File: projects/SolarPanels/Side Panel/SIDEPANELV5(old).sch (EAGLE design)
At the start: 31 parts

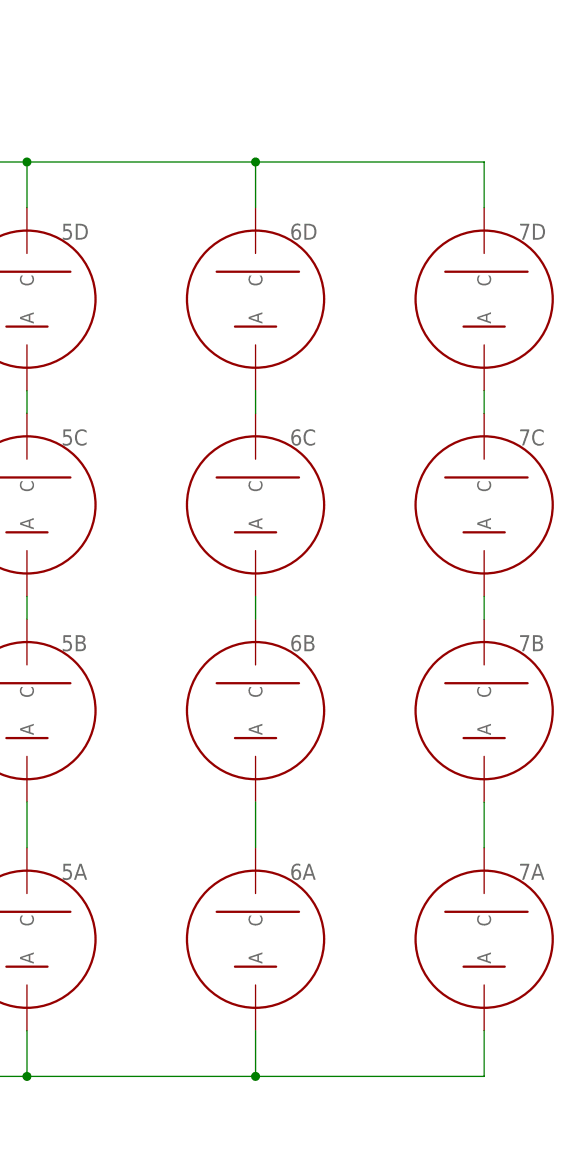
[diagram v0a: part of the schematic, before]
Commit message: side panel v5 WIP
updated cells
still figuring out cell layout
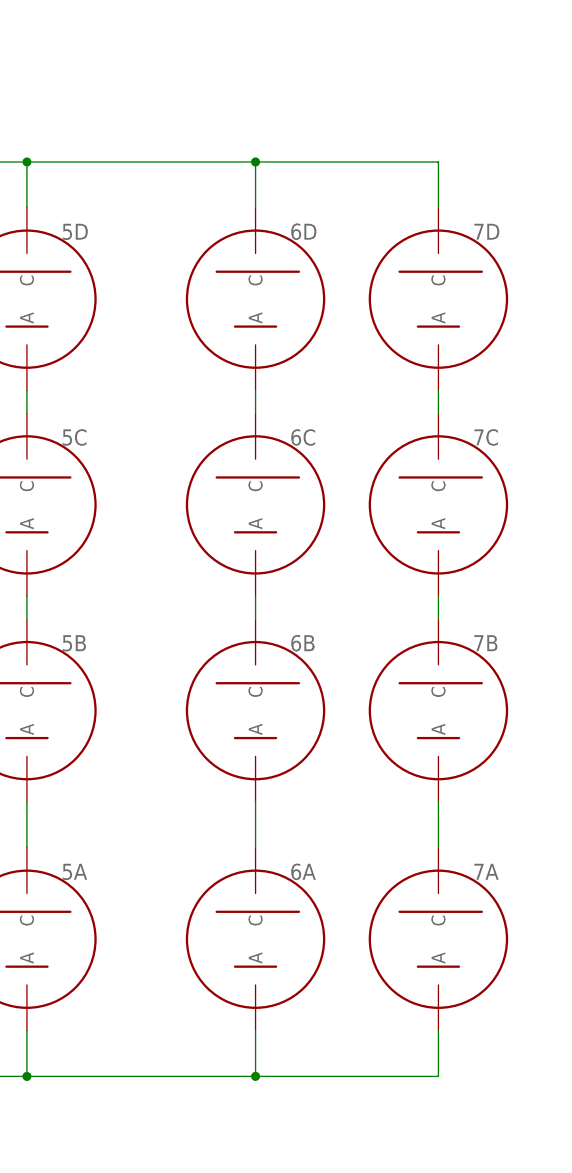
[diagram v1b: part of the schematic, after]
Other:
- moved on the sheet: 7A, 7B, 7C, 7D
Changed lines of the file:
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@@
 <?xml version="1.0" encoding="utf-8"?>
 <!DOCTYPE eagle SYSTEM "eagle.dtd">
-<eagle version="8.2.2">
+<eagle version="8.0.0">
 <drawing>
 <settings>
@@
 <instance part="6A" gate="G$1" x="17.78" y="-25.4"/>
 <instance part="PD" gate="G$1" x="-33.02" y="106.68"/>
-<instance part="7D" gate="G$1" x="43.18" y="45.72"/>
-<instance part="7C" gate="G$1" x="43.18" y="22.86"/>
-<instance part="7B" gate="G$1" x="43.18" y="0"/>
-<instance part="7A" gate="G$1" x="43.18" y="-25.4"/>
+<instance part="7D" gate="G$1" x="38.1" y="45.72"/>
+<instance part="7C" gate="G$1" x="38.1" y="22.86"/>
+<instance part="7B" gate="G$1" x="38.1" y="0"/>
+<instance part="7A" gate="G$1" x="38.1" y="-25.4"/>
 </instances>
 <busses>
@@
 <wire x1="-116.84" y1="-35.56" x2="-116.84" y2="-40.64" width="0.1524" layer="91"/>
 <pinref part="7A" gate="G$1" pin="A"/>
-<wire x1="17.78" y1="-40.64" x2="43.18" y2="-40.64" width="0.1524" layer="91"/>
-<wire x1="43.18" y1="-35.56" x2="43.18" y2="-40.64" width="0.1524" layer="91"/>
+<wire x1="38.1" y1="-35.56" x2="38.1" y2="-40.64" width="0.1524" layer="91"/>
+<wire x1="38.1" y1="-40.64" x2="17.78" y2="-40.64" width="0.1524" layer="91"/>
 <junction x="17.78" y="-40.64"/>
 </segment>
@@
 <wire x1="-60.96" y1="55.88" x2="-60.96" y2="60.96" width="0.1524" layer="91"/>
 <junction x="-60.96" y="60.96"/>
-<wire x1="17.78" y1="60.96" x2="43.18" y2="60.96" width="0.1524" layer="91"/>
+<junction x="17.78" y="60.96"/>
+<wire x1="17.78" y1="60.96" x2="38.1" y2="60.96" width="0.1524" layer="91"/>
+<wire x1="38.1" y1="60.96" x2="38.1" y2="55.88" width="0.1524" layer="91"/>
 <pinref part="7D" gate="G$1" pin="C"/>
-<wire x1="43.18" y1="55.88" x2="43.18" y2="60.96" width="0.1524" layer="91"/>
-<junction x="17.78" y="60.96"/>
 </segment>
 </net>
@@
 <pinref part="7D" gate="G$1" pin="A"/>
 <pinref part="7C" gate="G$1" pin="C"/>
-<wire x1="43.18" y1="35.56" x2="43.18" y2="33.02" width="0.1524" layer="91"/>
+<wire x1="38.1" y1="35.56" x2="38.1" y2="33.02" width="0.1524" layer="91"/>
 </segment>
 </net>
@@
 <pinref part="7C" gate="G$1" pin="A"/>
 <pinref part="7B" gate="G$1" pin="C"/>
-<wire x1="43.18" y1="12.7" x2="43.18" y2="10.16" width="0.1524" layer="91"/>
+<wire x1="38.1" y1="12.7" x2="38.1" y2="10.16" width="0.1524" layer="91"/>
 </segment>
 </net>
@@
 <pinref part="7B" gate="G$1" pin="A"/>
 <pinref part="7A" gate="G$1" pin="C"/>
-<wire x1="43.18" y1="-10.16" x2="43.18" y2="-15.24" width="0.1524" layer="91"/>
-</segment>
-</net>
+<wire x1="38.1" y1="-10.16" x2="38.1" y2="-15.24" width="0.1524" layer="91"/>
+</segment>
+</net>
